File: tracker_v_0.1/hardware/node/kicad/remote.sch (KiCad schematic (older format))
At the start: 13 parts, among them J1 Conn_Coaxial, J19 Conn_01x03_Female, J20 Conn_01x04_Female, J5 Conn_01x03_Female, Q1 Q_NMOS_GDS, U1 RFM95HW, U2 feather, U5 neo-6m-black

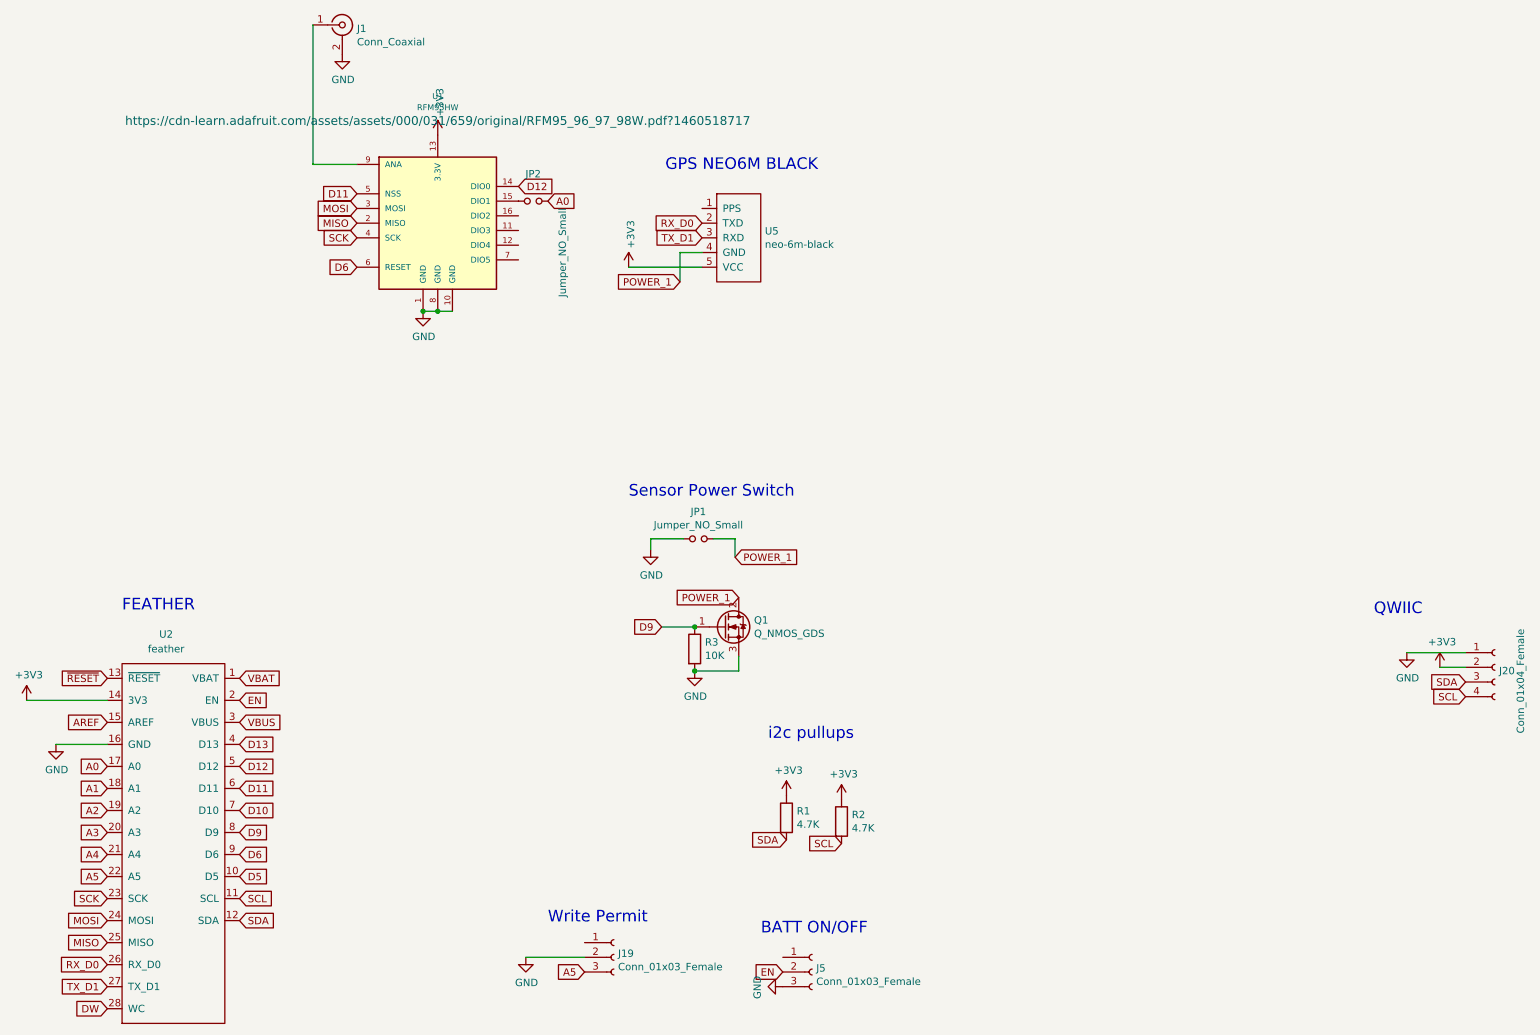
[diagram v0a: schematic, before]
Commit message: fully routed node
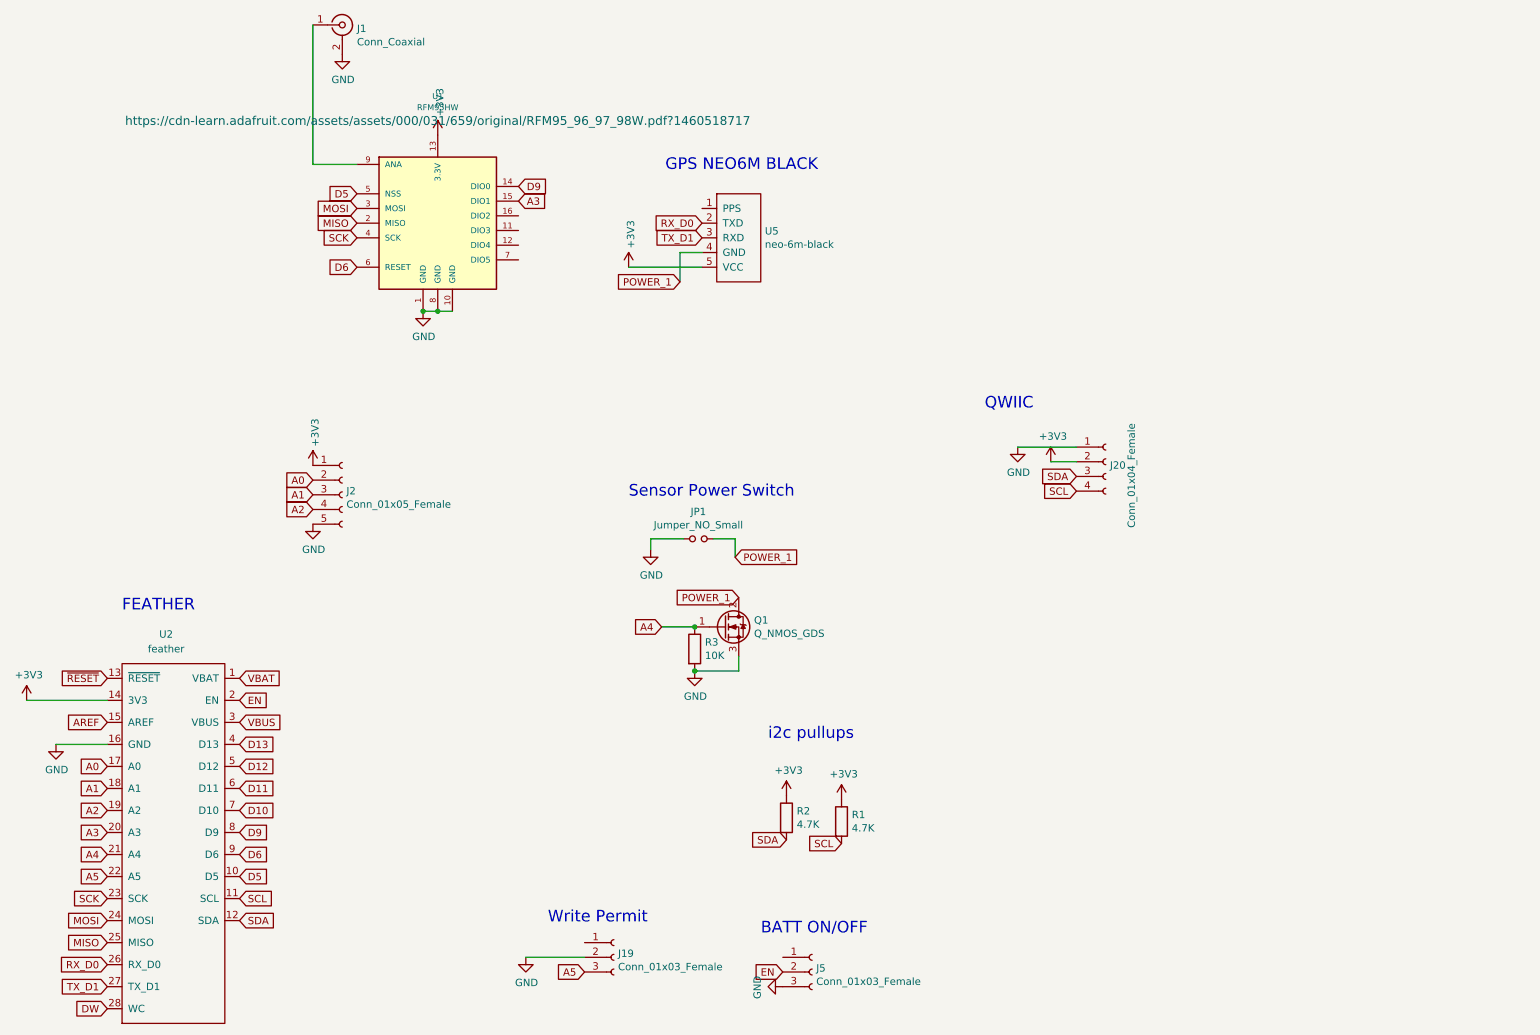
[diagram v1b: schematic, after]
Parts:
- removed JP2: Jumper_NO_Small, Jumper:SolderJumper-2_P1.3mm_Open_Pad1.0x1.5mm, symbol device:Jumper_NO_Small
- added J2: Conn_01x05_Female, Connector_PinSocket_2.54mm:PinSocket_1x05_P2.54mm_Vertical, symbol Connector:Conn_01x05_Female
- renumbered R2 to R1, R1 to R2
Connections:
- net +3V3: now also J2.1 (Pin_1)
- net A0: now also J2.2 (Pin_2)
- net A1: now also J2.3 (Pin_3)
- net A2: now also J2.4 (Pin_4)
- net A3: now also U1.15 (DIO1)
- net A4: now also Q1.1 (G), R3.1
- net D11: no longer U1.5 (NSS)
- net D12: no longer U1.14 (DIO0)
- net D5: now also U1.5 (NSS)
- net D9: now also U1.14 (DIO0); no longer Q1.1 (G), R3.1
- net GND: now also J2.5 (Pin_5)
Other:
- moved on the sheet: J20
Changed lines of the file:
@@
 $EndDescr
 $Comp
-L Device:R R1
+L Device:R R2
 U 1 1 5F989DB1
 P 5725 6150
-F 0 "R1" H 5795 6196 50  0000 L CNN
+F 0 "R2" H 5795 6196 50  0000 L CNN
 F 1 "4.7K" H 5795 6105 50  0000 L CNN
 F 2 "Resistor_THT:R_Axial_DIN0309_L9.0mm_D3.2mm_P12.70mm_Horizontal" V 5655 6150 50  0001 C CNN
@@
 $EndComp
 $Comp
-L Device:R R2
+L Device:R R1
 U 1 1 5F98BC9A
 P 6100 6175
-F 0 "R2" H 6170 6221 50  0000 L CNN
+F 0 "R1" H 6170 6221 50  0000 L CNN
 F 1 "4.7K" H 6170 6130 50  0000 L CNN
 F 2 "Resistor_THT:R_Axial_DIN0309_L9.0mm_D3.2mm_P12.70mm_Horizontal" V 6030 6175 50  0001 C CNN
@@
 Text GLabel 4350 7200 0    50   Input ~ 0
 A5
-Text Notes 9725 4775 0    79   ~ 0
+Text Notes 7075 3375 0    79   ~ 0
 QWIIC
 $Comp
 L Connector:Conn_01x04_Female J20
 U 1 1 61C7347D
-P 10550 5125
-F 0 "J20" H 10578 5101 50  0000 L CNN
-F 1 "Conn_01x04_Female" V 10725 4675 50  0000 L CNN
-F 2 "Connector_JST:JST_SH_SM04B-SRSS-TB_1x04-1MP_P1.00mm_Horizontal" H 10550 5125 50  0001 C CNN
-F 3 "~" H 10550 5125 50  0001 C CNN
-	1    10550 5125
-	1    0    0    -1
-$EndComp
-Wire Wire Line
-	10350 5125 10175 5125
-Wire Wire Line
-	10350 5025 9950 5025
-Text GLabel 10350 5325 0    50   Input ~ 0
+P 7900 3725
+F 0 "J20" H 7928 3701 50  0000 L CNN
+F 1 "Conn_01x04_Female" V 8075 3275 50  0000 L CNN
+F 2 "Connector_JST:JST_SH_SM04B-SRSS-TB_1x04-1MP_P1.00mm_Horizontal" H 7900 3725 50  0001 C CNN
+F 3 "~" H 7900 3725 50  0001 C CNN
+	1    7900 3725
+	1    0    0    -1
+$EndComp
+Wire Wire Line
+	7700 3725 7525 3725
+Wire Wire Line
+	7700 3625 7300 3625
+Text GLabel 7700 3925 0    50   Input ~ 0
 SCL
-Text GLabel 10350 5225 0    50   Input ~ 0
+Text GLabel 7700 3825 0    50   Input ~ 0
 SDA
 $Comp
 L power:+3V3 #PWR0112
 U 1 1 61C7348B
-P 10175 5125
-F 0 "#PWR0112" H 10175 4975 50  0001 C CNN
-F 1 "+3V3" H 10190 5298 50  0000 C CNN
-F 2 "" H 10175 5125 50  0001 C CNN
-F 3 "" H 10175 5125 50  0001 C CNN
-	1    10175 5125
+P 7525 3725
+F 0 "#PWR0112" H 7525 3575 50  0001 C CNN
+F 1 "+3V3" H 7540 3898 50  0000 C CNN
+F 2 "" H 7525 3725 50  0001 C CNN
+F 3 "" H 7525 3725 50  0001 C CNN
+	1    7525 3725
 	1    0    0    -1
 $EndComp
@@
 L power:GND #PWR0113
 U 1 1 61C73495
-P 9950 5025
-F 0 "#PWR0113" H 9950 4775 50  0001 C CNN
-F 1 "GND" H 9955 4852 50  0000 C CNN
-F 2 "" H 9950 5025 50  0001 C CNN
-F 3 "" H 9950 5025 50  0001 C CNN
-	1    9950 5025
+P 7300 3625
+F 0 "#PWR0113" H 7300 3375 50  0001 C CNN
+F 1 "GND" H 7305 3452 50  0000 C CNN
+F 2 "" H 7300 3625 50  0001 C CNN
+F 3 "" H 7300 3625 50  0001 C CNN
+	1    7300 3625
 	1    0    0    -1
 $EndComp
@@
 D6
 Text GLabel 3900 1850 2    50   Input ~ 0
-D12
+D9
 Text GLabel 2000 6100 2    50   Input ~ 0
 D10
@@
 	550  5350 1100 5350
 Text GLabel 2800 1900 0    50   Input ~ 0
-D11
+D5
 $Comp
 L Connector:Conn_01x03_Female J19
@@
 Connection ~ 3350 2700
 $Comp
-L device:Jumper_NO_Small JP2
-U 1 1 61E9417E
-P 4000 1950
-F 0 "JP2" H 4000 2135 50  0000 C CNN
-F 1 "Jumper_NO_Small" V 4200 1600 50  0000 C CNN
-F 2 "Jumper:SolderJumper-2_P1.3mm_Open_Pad1.0x1.5mm" H 4000 1950 50  0001 C CNN
-F 3 "" H 4000 1950 50  0001 C CNN
-	1    4000 1950
-	1    0    0    -1
-$EndComp
-Text GLabel 4100 1950 2    50   Input ~ 0
-A0
-$Comp
 L power:+3V3 #PWR0104
 U 1 1 6216FD88
@@
 $EndComp
 Text GLabel 4875 4850 0    50   Input ~ 0
-D9
+A4
 Connection ~ 5100 5150
 $Comp
@@
 	1    0    0    -1
 $EndComp
+Text GLabel 3900 1950 2    50   Input ~ 0
+A3
+$Comp
+L Connector:Conn_01x05_Female J2
+U 1 1 61EF5D35
+P 2700 3950
+F 0 "J2" H 2728 3976 50  0000 L CNN
+F 1 "Conn_01x05_Female" H 2728 3885 50  0000 L CNN
+F 2 "Connector_PinSocket_2.54mm:PinSocket_1x05_P2.54mm_Vertical" H 2700 3950 50  0001 C CNN
+F 3 "~" H 2700 3950 50  0001 C CNN
+	1    2700 3950
+	1    0    0    -1
+$EndComp
+$Comp
+L power:+3V3 #PWR0105
+U 1 1 61EF638E
+P 2500 3750
+F 0 "#PWR0105" H 2500 3600 50  0001 C CNN
+F 1 "+3V3" V 2515 3878 50  0000 L CNN
+F 2 "" H 2500 3750 50  0001 C CNN
+F 3 "" H 2500 3750 50  0001 C CNN
+	1    2500 3750
+	1    0    0    -1
+$EndComp
+$Comp
+L power:GND #PWR0106
+U 1 1 61EF71EC
+P 2500 4150
+F 0 "#PWR0106" H 2500 3900 50  0001 C CNN
+F 1 "GND" H 2505 3977 50  0000 C CNN
+F 2 "" H 2500 4150 50  0001 C CNN
+F 3 "" H 2500 4150 50  0001 C CNN
+	1    2500 4150
+	1    0    0    -1
+$EndComp
+Text GLabel 2500 3850 0    50   Input ~ 0
+A0
+Text GLabel 2500 3950 0    50   Input ~ 0
+A1
+Text GLabel 2500 4050 0    50   Input ~ 0
+A2
 $EndSCHEMATC
